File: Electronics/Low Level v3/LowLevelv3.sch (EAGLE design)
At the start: 53 parts, among them IC2 MCP4802, K1 ORWH-SH-105D1F,000, K3 ORWH-SH-105D1F,000, Q1 16MHz, T1 2N3904, T2 2N3904, U1 284512-4, U4 MCP2515, U5 MCP2551DIL08, X3 Motor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

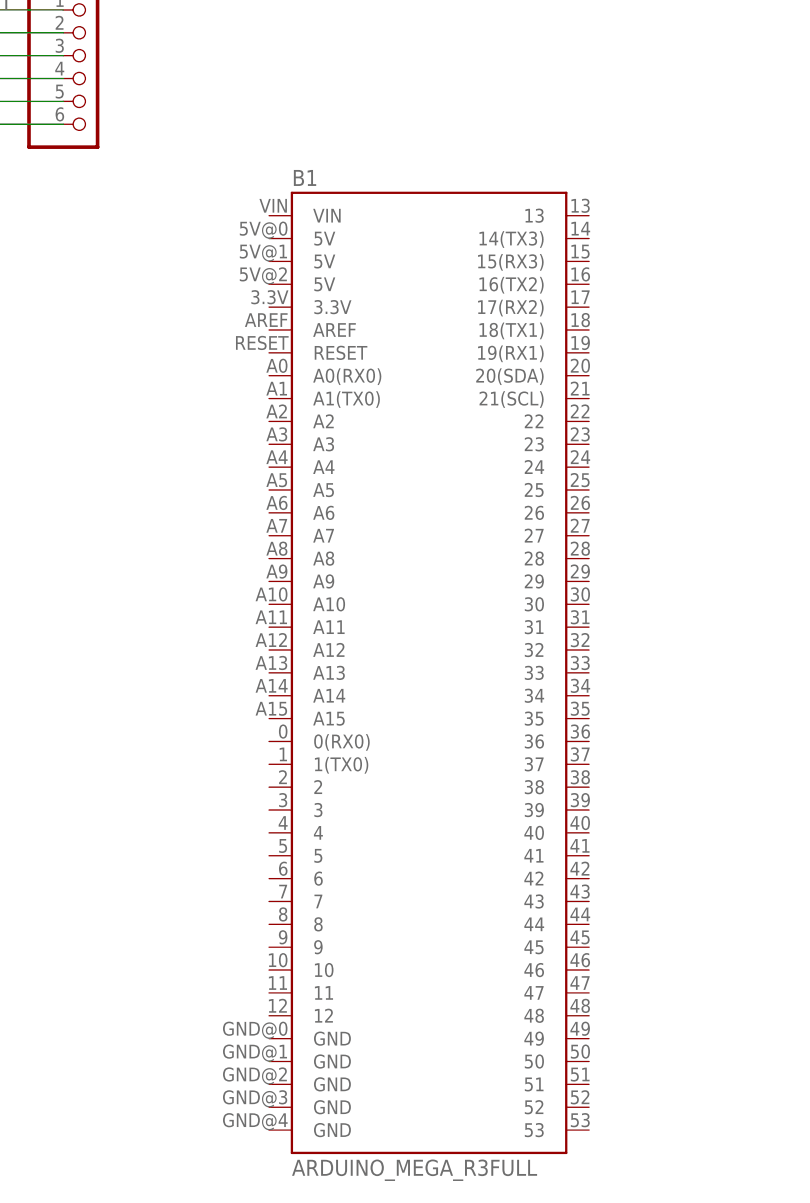
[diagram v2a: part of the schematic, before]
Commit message: removed accidental debugging Mega, added a handful of vias to fix GND orphans
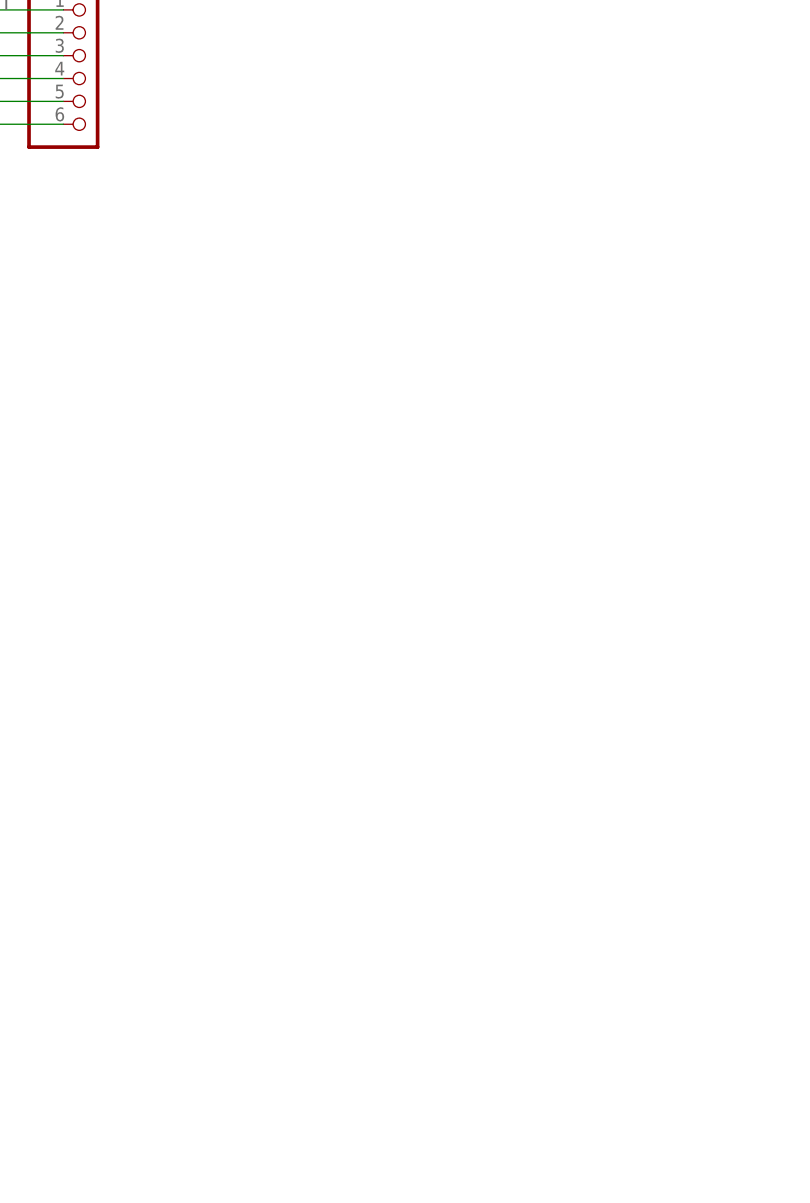
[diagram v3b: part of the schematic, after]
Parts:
- removed B1: ARDUINO_MEGA_R3FULL, SparkFun-Boards:ARDUINO_MEGA_R3FULL
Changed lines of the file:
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@@
 <part name="J1" library="SparkFun-Connectors" library_urn="urn:adsk.eagle:library:513" deviceset="CONN_03" device="-SCREW-5MM" package3d_urn="urn:adsk.eagle:package:38070/1"/>
 <part name="R12" library="rcl" library_urn="urn:adsk.eagle:library:334" deviceset="R-US_" device="0207/10" package3d_urn="urn:adsk.eagle:package:23491/2" value="120"/>
-<part name="B1" library="SparkFun-Boards" library_urn="urn:adsk.eagle:library:509" deviceset="ARDUINO_MEGA_R3" device="FULL" package3d_urn="urn:adsk.eagle:package:37320/1"/>
 </parts>
 <sheets>
@@
 <attribute name="VALUE" x="147.32" y="206.502" size="1.778" layer="96" rot="R180"/>
 </instance>
-<instance part="B1" gate="G$1" x="139.7" y="-43.18" smashed="yes">
-<attribute name="NAME" x="124.46" y="10.922" size="1.778" layer="95"/>
-<attribute name="VALUE" x="124.46" y="-99.06" size="1.778" layer="96"/>
-</instance>
 </instances>

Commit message: schematic cleanup
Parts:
- removed COMM_DIG: DIG 14-21, pinhead:PINHD-1X8
- removed D8-13: PWMH, pinhead:PINHD-1X8
- removed PWML: Digital 0-7, pinhead:PINHD-1X8
- added DIGITAL_0-7: Digital 0-7, pinhead:PINHD-1X8
- added DIGITAL_14-21: Digital 14-21, pinhead:PINHD-1X8
- added DIGITAL_8-13: Digital 8-13, pinhead:PINHD-1X8
- MEGA_EXPANSION: value D22-D53 -> Digital 22-53
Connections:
- net 3MISO: now also DIGITAL_8-13.5; no longer D8-13.5
- net 3MOSI: now also DIGITAL_8-13.4; no longer D8-13.4
- net EBIKECONTRL: now also DIGITAL_14-21.4; no longer COMM_DIG.4
- net HALLPHASEA: now also DIGITAL_14-21.1; no longer COMM_DIG.1
- net HALLPHASEB: now also DIGITAL_14-21.2; no longer COMM_DIG.2
- net HALLPHASEC: now also DIGITAL_14-21.3; no longer COMM_DIG.3
- net RX3: now also DIGITAL_14-21.7; no longer COMM_DIG.7
- net SCK: now also DIGITAL_8-13.6; no longer D8-13.6
- net SPEEDOMETER: now also DIGITAL_0-7.3; no longer PWML.3
- net STEER_SERVO_PWM: now also DIGITAL_8-13.1; no longer D8-13.1
- net TX3: now also DIGITAL_14-21.8; no longer COMM_DIG.8
- net WATCHDOG: now also DIGITAL_0-7.6; no longer PWML.6
- net WHEELROTATION: now also DIGITAL_0-7.4; no longer PWML.4
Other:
- moved on the sheet: 24V_ACTIVE, ADCL, BRAKES_ON, C1, C10, C11, C13, C2, C3, C4, C5, C6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

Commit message: rearranged silkscreen for clarity in v3
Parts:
- added B1: ARDUINO_MEGA_R3FULL, SparkFun-Boards:ARDUINO_MEGA_R3FULL
- renumbered STEERING_SENSE to STEERING_IO

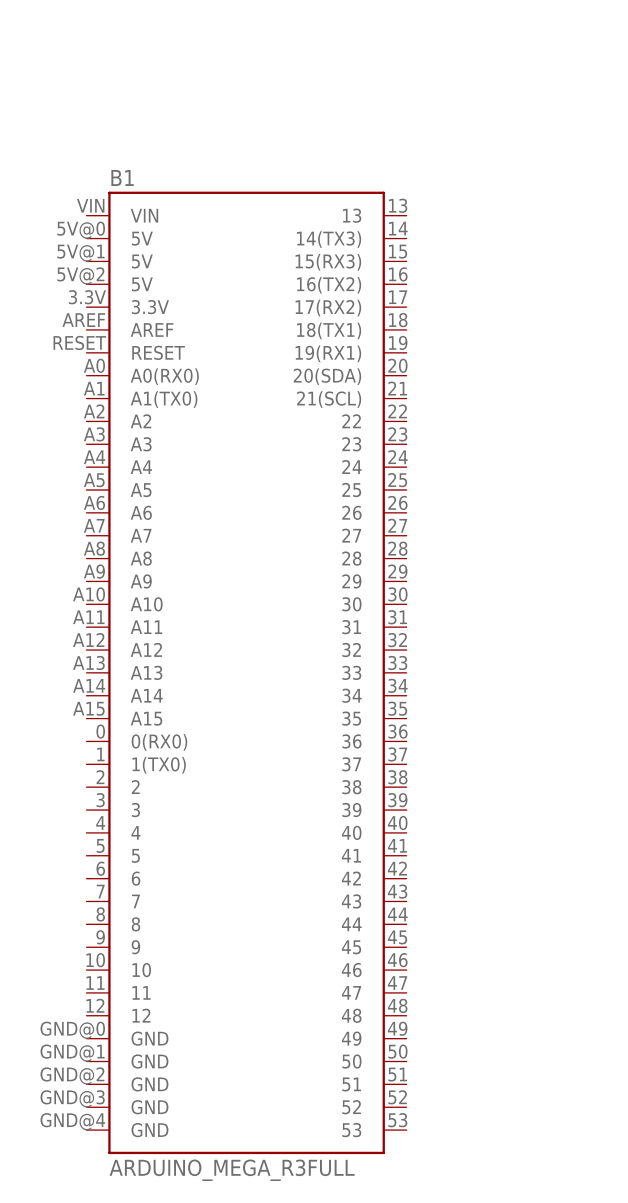
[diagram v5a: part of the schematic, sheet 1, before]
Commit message: Added reset button to top of board
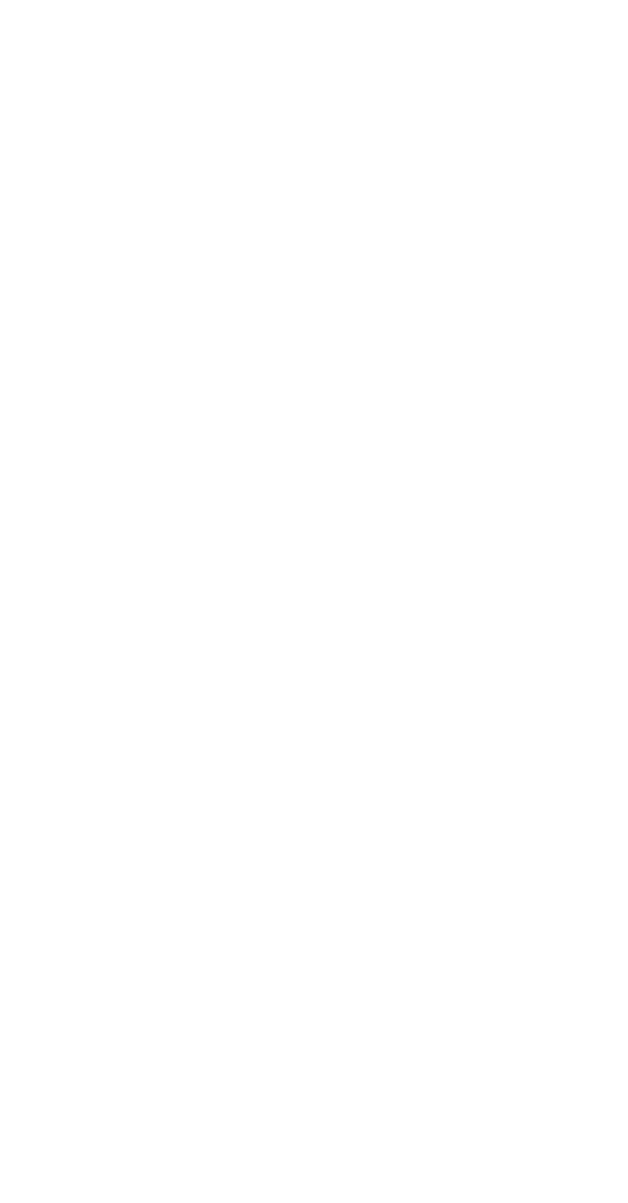
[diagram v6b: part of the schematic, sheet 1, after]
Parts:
- removed B1: ARDUINO_MEGA_R3FULL, SparkFun-Boards:ARDUINO_MEGA_R3FULL
- added R13: 1K, rcl:R-US_0207/10
- added RESET: MOMENTARY-SWITCH-SPST-PTH-6.0MM, SparkFun-Switches:MOMENTARY-SWITCH-SPST-PTH-6.0MM
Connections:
- new net N$1: R13.2, RESET.2
- net GND: now also R13.1
- net RESET: now also RESET.1
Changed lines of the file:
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@@
 <part name="FRAME1" library="frames" library_urn="urn:adsk.eagle:library:229" deviceset="A4L-LOC" device=""/>
 <part name="FRAME2" library="frames" library_urn="urn:adsk.eagle:library:229" deviceset="A4L-LOC" device=""/>
-<part name="B1" library="SparkFun-Boards" library_urn="urn:adsk.eagle:library:509" deviceset="ARDUINO_MEGA_R3" device="FULL" package3d_urn="urn:adsk.eagle:package:37320/1"/>
+<part name="RESET" library="SparkFun-Switches" library_urn="urn:adsk.eagle:library:535" deviceset="MOMENTARY-SWITCH-SPST" device="-PTH-6.0MM" package3d_urn="urn:adsk.eagle:package:40163/1"/>
+<part name="R13" library="rcl" library_urn="urn:adsk.eagle:library:334" deviceset="R-US_" device="0207/10" package3d_urn="urn:adsk.eagle:package:23491/2" value="1K"/>
 </parts>
 <sheets>
@@
 <attribute name="SHEET" x="230.505" y="5.08" size="2.54" layer="94"/>
 </instance>
-<instance part="B1" gate="G$1" x="45.72" y="-99.06" smashed="yes">
-<attribute name="NAME" x="30.48" y="-44.958" size="1.778" layer="95"/>
-<attribute name="VALUE" x="30.48" y="-154.94" size="1.778" layer="96"/>
-</instance>
 </instances>
 <busses>
@@
 <attribute name="LAST_DATE_TIME" x="217.17" y="10.16" size="2.286" layer="94"/>
 <attribute name="SHEET" x="230.505" y="5.08" size="2.54" layer="94"/>
+</instance>
+<instance part="RESET" gate="G$1" x="175.26" y="71.12" smashed="yes">
+<attribute name="NAME" x="175.26" y="72.644" size="1.778" layer="95" font="vector" align="bottom-center"/>
+<attribute name="VALUE" x="175.26" y="70.612" size="1.778" layer="96" font="vector" align="top-center"/>
+</instance>
+<instance part="R13" gate="G$1" x="184.15" y="71.12" smashed="yes" rot="R180">
+<attribute name="NAME" x="187.96" y="69.6214" size="1.778" layer="95" rot="R180"/>
+<attribute name="VALUE" x="187.96" y="74.422" size="1.778" layer="96" rot="R180"/>
 </instance>
 </instances>
@@
 <pinref part="R11" gate="G$1" pin="2"/>
 </segment>
+<segment>
+<pinref part="R13" gate="G$1" pin="1"/>
+<wire x1="189.23" y1="71.12" x2="198.12" y2="71.12" width="0.1524" layer="91"/>
+<label x="193.04" y="71.12" size="1.778" layer="95"/>
+</segment>
 </net>
 <net name="SELECTAB" class="0">
@@
 </segment>
 </net>
+<net name="RESET" class="0">
+<segment>
+<pinref part="RESET" gate="G$1" pin="1"/>
+<wire x1="170.18" y1="71.12" x2="160.02" y2="71.12" width="0.1524" layer="91"/>
+<label x="160.02" y="71.12" size="1.778" layer="95"/>
+</segment>
+</net>
+<net name="N$1" class="0">
+<segment>
+<pinref part="R13" gate="G$1" pin="2"/>
+<pinref part="RESET" gate="G$1" pin="2"/>
+<wire x1="179.07" y1="71.12" x2="180.34" y2="71.12" width="0.1524" layer="91"/>
+</segment>
+</net>

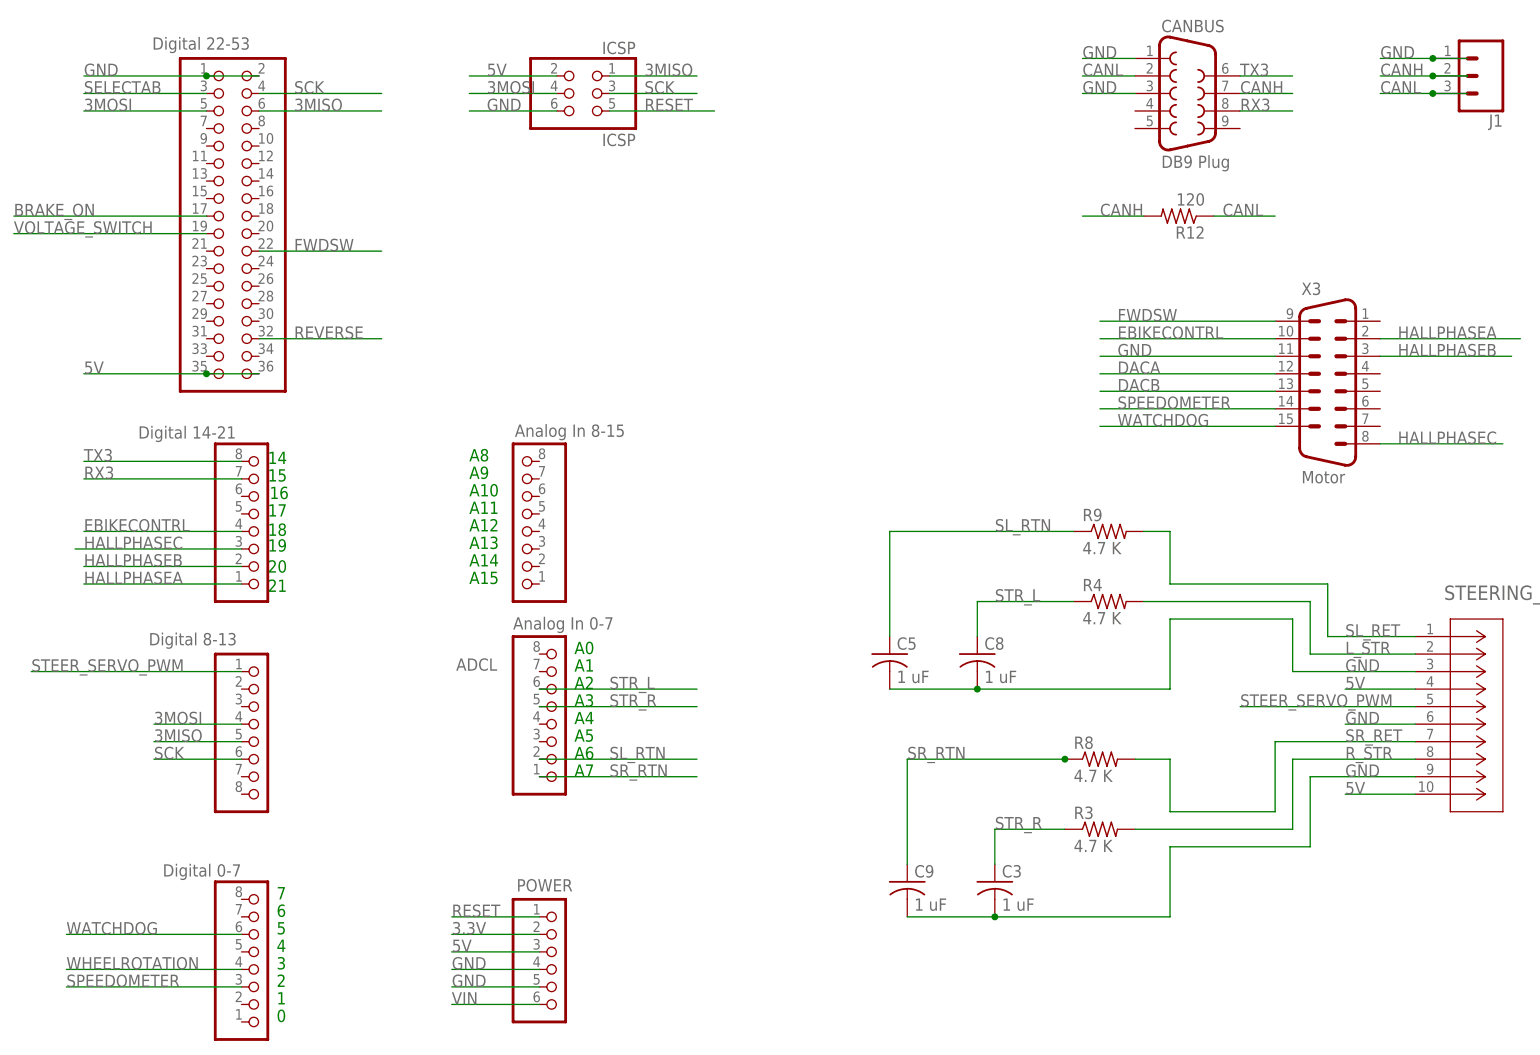
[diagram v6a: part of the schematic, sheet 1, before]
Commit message: Many LLBv3 updates in one!
re-arranged inerrupt pins to share a PCI ISR, added RC circuit to MCP2515 per datasheet, replaced impossible capacitor, re-arranged oscilator layout
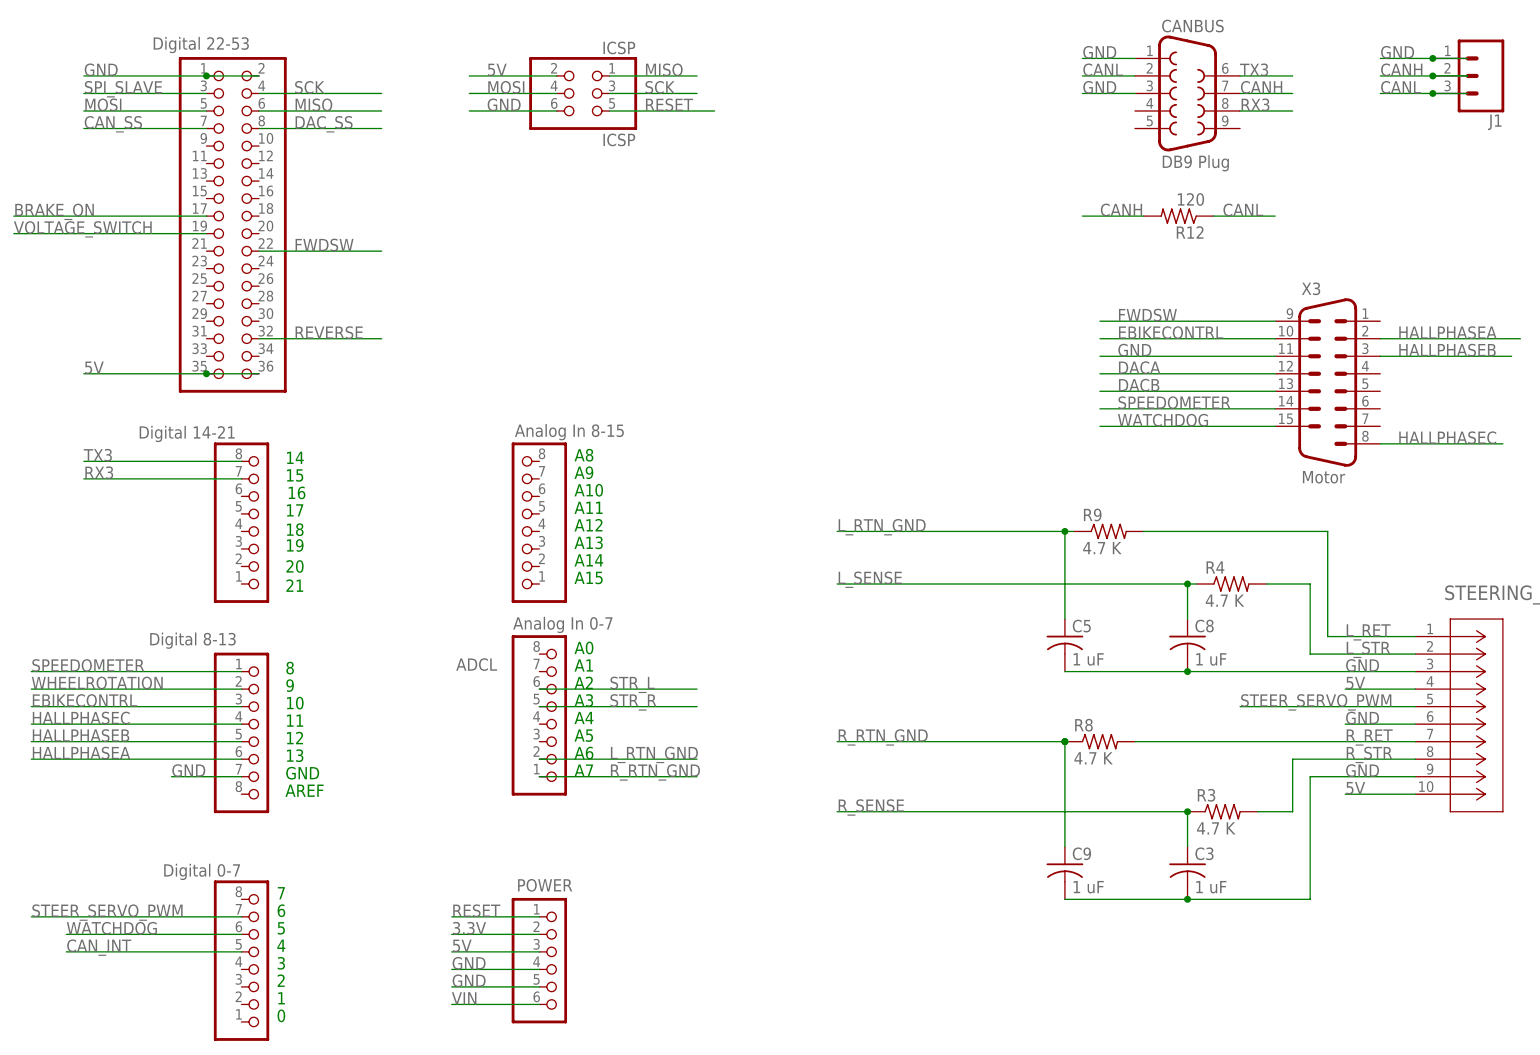
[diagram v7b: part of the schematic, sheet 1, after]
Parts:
- added C12, C14: 0.1uF, rcl:C-US025-025X050
- added R14: 1K, rcl:R-US_0207/10
- added R15: 20K, rcl:R-US_0207/10
- C11, C6: value 22pF -> 33pF
- C2: value 0.2uF -> 0.1uF
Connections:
- net SL_RET renamed L_RET
- net SL_RTN renamed L_RTN_GND
- net SR_RET renamed R_RET
- net SR_RTN renamed R_RTN_GND
- removed net 3MISO: DIGITAL_8-13.5, ICSP.1, MEGA_EXPANSION.6
- removed net 3MOSI: DIGITAL_8-13.4, IC2.4, ICSP.4, MEGA_EXPANSION.5
- removed net CAN_CS: U4>NAME.CS
- removed net SELECTAB: IC2.2, MEGA_EXPANSION.3
- new net CAN_SS: MEGA_EXPANSION.7, U4>NAME.CS
- new net DAC_SS: IC2.2, MEGA_EXPANSION.8
- new net L_SENSE: C8.1, R4.1
- new net N$4: C14.1, R14.2, R15.2
- new net R_SENSE: C3.1, R3.1
- new net SPI_SLAVE: MEGA_EXPANSION.3
- net 5V: now also C12.1, R15.1
- net CAN_INT: now also DIGITAL_0-7.5
- net EBIKECONTRL: now also DIGITAL_8-13.3; no longer DIGITAL_14-21.4
- net GND: now also C12.2, C14.2, DIGITAL_8-13.7
- net HALLPHASEA: now also DIGITAL_8-13.6; no longer DIGITAL_14-21.1
- net HALLPHASEB: now also DIGITAL_8-13.5; no longer DIGITAL_14-21.2
- net HALLPHASEC: now also DIGITAL_8-13.4; no longer DIGITAL_14-21.3
- net MISO: now also ICSP.1, MEGA_EXPANSION.6
- net MOSI: now also IC2.4, ICSP.4, MEGA_EXPANSION.5
- net RS: now also R14.1
- net SCK: no longer DIGITAL_8-13.6
- net SPEEDOMETER: now also DIGITAL_8-13.1; no longer DIGITAL_0-7.3
- net STEER_SERVO_PWM: now also DIGITAL_0-7.7; no longer DIGITAL_8-13.1
- net STR_L: no longer C8.1, R4.1
- net STR_R: no longer C3.1, R3.1
- net WHEELROTATION: now also DIGITAL_8-13.2; no longer DIGITAL_0-7.4
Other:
- note added: "10"
- note added: "11"
- note added: "12"
- note added: "13"
- note added: "8"
- note added: "9"
- note added: "AREF"
- note added: "GND"
- moved on the sheet: C3, C5, C8, C9, R3, R4, R8

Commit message: LLBv3 updates
replaced all thru-hole res/cap with SMD parts, arranged part grids, re-routed the board
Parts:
- C1, C10, C11, C12, C13, C14, C2, C6, C7: device rcl:C-US025-025X050 -> resistor:C-USC1206
- C3, C4, C5, C8, C9: device rcl:C-US025-030X050 -> resistor:C-USC1206
- R1, R10, R11, R12, R13, R14, R15, R2, R3, R4, R5, R6, R7, R8, R9: device rcl:R-US_0207/10 -> resistor:R-US_R1206
